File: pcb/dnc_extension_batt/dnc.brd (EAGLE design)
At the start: 97.2 x 88 mm, 132 parts, among them IC1 LM2596S, IC2 74S244DW, Q1 IRF9321PBF, Q10 BSS316, Q11 BSS316, Q12 BSS138, Q13 BSS138, Q2 BSS670, Q3 BSS138, Q4 BSS670, Q5 BSS138, Q6 BSS670, Q7 BSS138, Q8 BSS138, Q9 BSS670, U1 MAX202CDWR, U2 74HCT595D, U3 TC7SU04F, U4 AL8807, U5 AL8807, U6 TC7SU04F

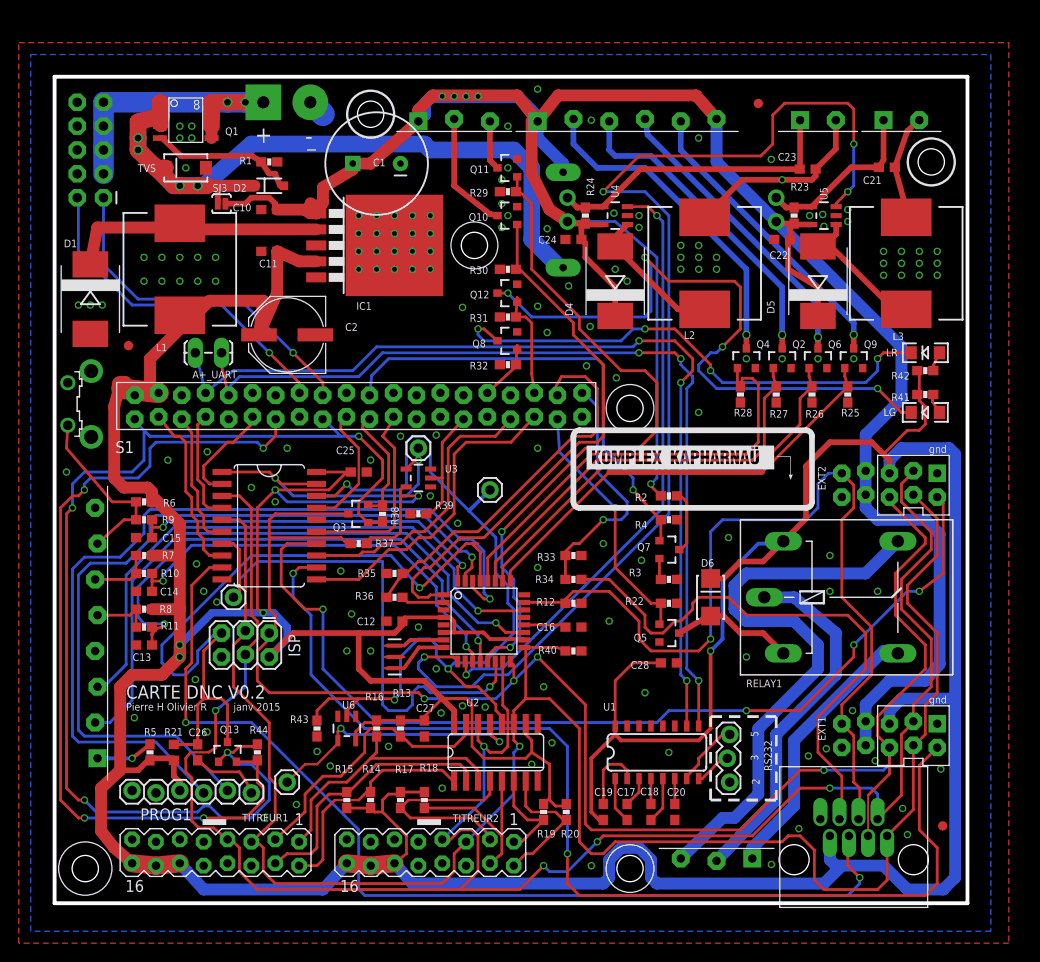
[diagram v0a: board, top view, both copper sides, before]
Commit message: carte extension chargeur LIPO
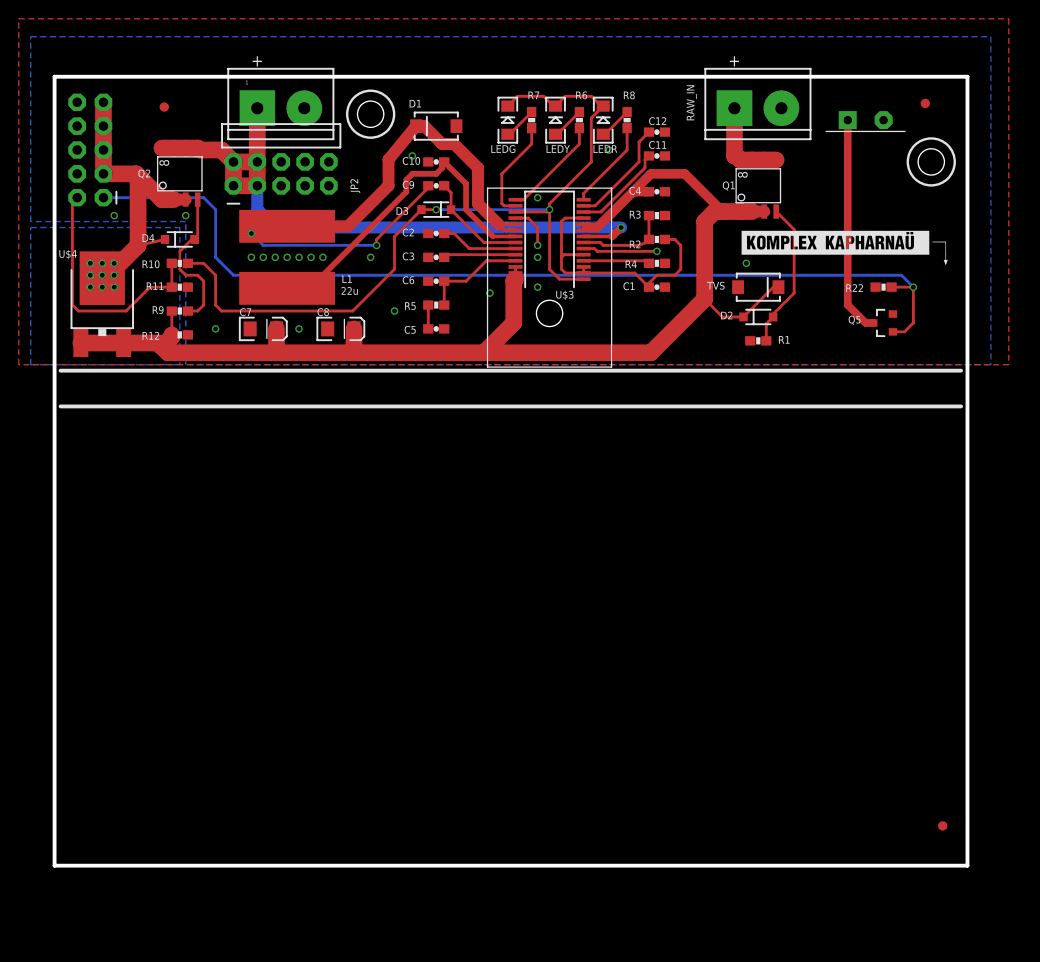
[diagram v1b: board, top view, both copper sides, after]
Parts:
- removed 16MHZ: 16MHZ, SparkFun-FreqCtrl:RESONATOR-SMD
- removed A+_UART: (no value), SparkFun:1X02_LOCK_LONGPADS
- removed AT328: ATMEGA328, SparkFun:TQFP32-08
- removed C13, C14, C15, C21, C23: 1uF, rcl:C0603
- removed C16, C17, C18, C19, C20, C22, C24, C25, C26, C27, C28: 0.1uF, rcl:C0603
- removed D5: 40v5A, diode:SMC
- removed D6: (no value), SparkFun-DiscreteSemi:SMA-DIODE_ALT
- removed EXT1: EXT1, pierre_vv:EXTPINDNC
- removed EXT2: EXT2, pierre_vv:EXTPINDNC
- removed F1: 8A, SparkFun:PTC
- removed IC1: LM2596S, national-semiconductor:TO263-5
- removed IC2: 74S244DW, 74xx-us:SO20W
- removed ISP: AVR_SPI_PRG_62X3_LOCK, SparkFun:2X3_LOCK
- removed JP3: atmega cs, SparkFun-Connectors:1X01
- removed JP4: allcs, SparkFun-Connectors:1X01
- removed JP5: OE 595, SparkFun-Connectors:1X01
- removed L2, L3: 100nH, SparkFun:CDRH125
- removed LG, LR: (no value), SparkFun-LED:LED-1206
- removed PLUG_3.81_1: FLEX, pierre_vv:PLUG_03
- removed PLUG_3.81_2: RELAY, pierre_vv:PLUG_03
- removed PLUG_3.81_2_2: LED10W1, pierre_vv:PLUG_02
- removed PLUG_3.81_6_1: GYRO LED, pierre_vv:PLUG_06
- removed PROG1: (no value), SparkFun:1X06_LOCK
- removed Q10, Q11: BSS316, SparkFun-DiscreteSemi:SOT23-3
- removed Q12, Q13, Q3, Q7, Q8: BSS138, SparkFun-DiscreteSemi:SOT23-3
- removed Q4, Q6, Q9: BSS670, SparkFun-DiscreteSemi:SOT23-3
- removed R13, R14, R15, R16, R17, R18, R19, R20, R25, R26, R27, R28, R29, R30, R31, R32: 100K, SparkFun-Passives:0603-RES
- removed R21: 10K, rcl:R0603
- removed R23, R24: 0.110, SparkFun-Passives:0603-RES
- removed R33, R35: 20K, SparkFun-Passives:0603-RES
- removed R34, R36, R37, R38, R39, R40, R43, R44: 10K, SparkFun-Passives:0603-RES
- removed R41, R42: 220, SparkFun-Passives:0603-RES
- removed RELAY1: G5L, relay:G5LE
- removed RS232: (no value), SparkFun-Connectors:1X03_LOCK
- removed S1: (no value), switch-omron:B3F-31XX
- removed SJ1, SJ2: JUMPER-PTH-2-NO, SparkFun-Passives:PTH-JUMPER-2-NO_NO_SILK
- removed SJ3: JUMPER-PAD-2-NC_BY_PASTE, SparkFun-Passives:PAD-JUMPER-2-NC_BY_PASTE_YES_SILK
- removed TITREUR1, TITREUR2: DNC_TITREUR, pierre_vv:DNC_TITREUR
- removed U$6: M08, pierre_vv:PLUG_08
- removed U$8: RJ45-EXTDNC, con-amphenol-rj45-ld:RJ45-TRAFO
- removed U1: MAX202CDWR, SparkFun-DigitalIC:SO016
- removed U2: 74HCT595D, IC:SO16
- removed U3, U6: TC7SU04F, SparkFun-DigitalIC:SOT23-5
- removed U4, U5: AL8807, SparkFun-PowerIC:SOT23-5
- added 1: BATT, pierre_vv:DNC_IN2_PWR
- added C3, C4, C5, C9: 0.1u, SparkFun-Passives:0603-CAP
- added C6: 1n, SparkFun-Passives:0603-CAP
- added C7, C8: 22u, SparkFun-Passives:EIA3216
- added D3: 1N4148W, SparkFun-DiscreteSemi:SOD-123
- added LEDG, LEDR, LEDY: (no value), SparkFun-LED:LED-1206
- added U$3: MAX1758, pierre_vv:SSOP28
- C1: value 680uF30mm -> 1u; device SparkFun:CPOL-RADIAL-1000UF-25V -> SparkFun-Passives:0603-CAP
- C10: value 0.1uF -> 0.1u; device rcl:C0603 -> SparkFun-Passives:0603-CAP
- C11: value 0.1uF -> 2.2n; device rcl:C0603 -> SparkFun-Passives:0603-CAP
- C12: value 0.1uF -> 4.7n; device rcl:C0603 -> SparkFun-Passives:0603-CAP
- C2: value 220u -> 0.1u; device rcl:PANASONIC_E -> SparkFun-Passives:0603-CAP
- D1: value 40v5A -> B330; device diode:SMC -> SparkFun-DiscreteSemi:SMA-DIODE
- D2: value 10V -> 10v
- D4: value 40v5A -> 10v; device diode:SMC -> SparkFun-DiscreteSemi:SOD-123
- JP2: value regrck -> BATT; device SparkFun-Connectors:1X01 -> SparkFun-Connectors:2X5-RA
- L1: value 68nH3A -> 22u; device SparkFun:CDRH125 -> pierre_vv:SRN1060
- PLUG_3.81_2_1: value LED10W2 -> RELAY-SINK
- Q2: value BSS670 -> IRF9321PBF; device SparkFun-DiscreteSemi:SOT23-3 -> pierre_vv:SO-8
- R10, R11: value 33K -> 10K
- R12: value (none) -> 10K
- R2: value 100k1% -> 100K1%
- R3: value 10k1% -> 100K1%
- R4: value 100K -> 10K
- R5: value 1K -> 10K
- R6, R7, R8: value 56K -> 1K
- R9: value 33K -> 100K
- RAW_IN: value DNC_IN2PWR -> SUPPLY
- U$4: value RASPIA+ -> 45V10A; device pierre_vv:RASPIA+ -> pierre_vv:DPAK
- moved U$4 88.1 mm to (5.08, 61.0), turned to 0 degrees
- moved R8 73.2 mm to (61.0, 79.4), turned to 90 degrees
- moved Q2 67.1 mm to (13.3, 73.7), turned to 90 degrees
- moved TVS 62.3 mm to (74.9, 61.6), turned to 0 degrees
- moved R7 62.1 mm to (50.8, 79.4), turned to 90 degrees
- moved R6 61.6 mm to (55.9, 79.4), turned to 90 degrees
- moved Q1 61.4 mm to (74.9, 72.4), turned to 90 degrees
- moved C12 59.1 mm to (64.1, 78.1), turned to 0 degrees
- moved R5 56.5 mm to (40.6, 59.7), turned to 0 degrees
- moved R1 55.4 mm to (74.9, 55.9), turned to 180 degrees
- moved D2 53.9 mm to (74.9, 58.4)
- moved R12 50.7 mm to (13.3, 56.5)
- moved RAW_IN 50.2 mm to (72.4, 80.6), flipped to the top, turned to 0 degrees
- moved D4 46.6 mm to (13.3, 66.7), turned to 0 degrees
- moved C11 42.5 mm to (64.1, 75.6), turned to 0 degrees
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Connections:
- removed net +3V3: Q13.1, Q3.1, R38.2, R44.2, U$4.1, U$4.17
- removed net +5V: AT328.18, AT328.4, AT328.6, C11.1, C12.1, C19.1, C2.+, C25.1, C27.1, C28.1, D6.C, EXT1.5V, EXT2.5V, IC1.4, IC2.20, ISP.2, L1.2, PROG1.4, R13.2, R14.2, R15.2, R16.2, R17.2, R18.2, R19.2, R20.2, R21.2, R37.2, R41.2, R42.2, R5.2, R6.2, R7.2, R8.2, RELAY1.2, TITREUR1.12, TITREUR1.14, TITREUR1.16, TITREUR2.12, TITREUR2.14, TITREUR2.16, U$4.2, U$4.4, U$8.1, U1.16, U2.10, U2.16, U3.5, U6.5
- removed net /REG_RCK_5V=ACTIVE_CS: JP5.1, U2.13, U6.4
- removed net ALL_CS_ENABLE_ACTIVE_LOW_5V: IC2.1, IC2.19, JP4.1, U3.4
- removed net ANALOG_BAT: AT328.24
- removed net ANALOG_RAW: Q7.2, R3.2
- removed net AREF: AT328.20, C16.1
- removed net ATMEGA_CS: IC2.13, U$4.33
- removed net ATMEGA_CS_5V: AT328.14, IC2.7, JP3.1
- removed net CODE: AT328.23, EXT1.RETOURANALOG, EXT2.RETOURANALOG, R12.1, U$8.6
- removed net CS_TRIGGER_ACTIVE_HIGH: R39.2, U$4.29, U3.2
- removed net DTR: C26.1, PROG1.1
- removed net EXT1_CS: IC2.8, U$4.3
- removed net EXT1_CS_5V: EXT1./CS, IC2.12
- removed net EXT2_CS: IC2.6, U$4.5
- removed net EXT2_CS_5V: EXT2./CS, IC2.14
- removed net EXT3_CS: IC2.4, U$4.7
- removed net EXT3_CS_5V: IC2.16
- removed net FLOAT1: AT328.19, U$6.2
- removed net FLOAT2: AT328.22, U$6.3
- removed net GYRO_1: AT328.28, Q4.1, R28.2
- removed net GYRO_2: AT328.27, Q2.1, R27.2
- removed net GYRO_3: AT328.26, Q6.1, R26.2
- removed net GYRO_4: AT328.25, Q9.1, R25.2
- removed net INT_ATMEGA: R35.2, R36.1, U$4.38
- removed net INT_ATMEGA_5V: AT328.2, R36.2
- removed net INT_TELECO: R33.2, R34.1, U$4.40
- removed net INT_TELECO_5V: R34.2, U$8.4
- removed net LED+1: C23.1, PLUG_3.81_2_1.1, R24.1, SJ1.2, U4.4
- removed net LED+2: C21.1, PLUG_3.81_2_2.1, R23.1, SJ2.2, U5.4
- removed net LED-1: C23.2, L2.2, PLUG_3.81_2_1.2
- removed net LED-2: C21.2, L3.2, PLUG_3.81_2_2.2
- removed net LEDR: LR.C, Q8.3
- removed net LED_G: Q12.1, R31.2, U$4.36
- removed net LED_R: Q8.1, R32.2, U$4.32
- removed net LG: LG.C, Q12.3
- removed net MISO: Q3.2, R38.1, U$4.21
- removed net MISO_5V: AT328.16, EXT1.MISO, EXT2.MISO, ISP.1, Q3.3, R37.1, U$8.5
- removed net MOSI: IC2.17, U$4.19
- removed net MOSI_5V: AT328.15, EXT1.MOSI, EXT2.MOSI, IC2.3, ISP.4, TITREUR1.7, TITREUR2.7, U$8.8, U2.14
- removed net N$22: R6.1, R9.1, S1.2, U$6.7
- removed net N$23: R11.1, R8.1, U$6.5
- removed net N$24: C19.2, U1.2
- removed net N$25: R5.1, U$6.1
- removed net N$35: C20.1, U1.6
- removed net N$43: 16MHZ.1, AT328.7
- removed net N$44: 16MHZ.3, AT328.8
- removed net N$50: C18.2, U1.5
- removed net N$51: C18.1, U1.4
- removed net N$52: C17.2, U1.3
- removed net N$53: C17.1, U1.1
- removed net PRXD_PIN2_RS232: RS232.1, U1.7
- removed net PTXD_PIN3_RS232: RS232.2, U1.8
- removed net PUSH1: AT328.32, C15.1, R9.2
- removed net PUSH2: AT328.11, C14.1, R10.2
- removed net PUSH3: AT328.12, C13.1, R11.2
- removed net PWM_FLEX_1: AT328.1, Q10.1, R30.2
- removed net PWM_FLEX_2: AT328.13, Q11.1, R29.2
- removed net PWM_LED_1: AT328.9, U5.3
- removed net PWM_LED_2: AT328.10, U4.3
- removed net RAW_FUSED: C1.1, C10.1, C22.1, C24.1, D4.C, D5.C, EXT1.RAW, EXT1.RAW2, EXT2.RAW, EXT2.RAW2, F1.P$2, IC1.1, PLUG_3.81_1.1, PLUG_3.81_6_1.1, PLUG_3.81_6_1.6, R2.2, R23.2, R24.2, SJ1.1, SJ2.1, SJ3.2, U4.5, U5.5
- removed net RAW_UNPROTECTED: JP1.3, JP1.5, JP1.7, JP1.9, Q1.5, Q1.6, Q1.7, Q1.8, RAW_IN.1
- removed net READ_BATTERY: Q7.1, R4.2, U$4.22
- removed net REG_RCK: IC2.2, U$4.11
- removed net REG_RCK_5V: IC2.18, JP2.1, R43.2, U2.12, U6.2
- removed net RELAY1: Q5.1, R22.2, U$4.37
- removed net RESET: Q13.2, R44.1, U$4.13
- removed net RESET_5V: AT328.29, C26.2, ISP.5, Q13.3, R21.1
- removed net RST1: R16.1, TITREUR1.1, U2.3
- removed net RST2: R14.1, TITREUR1.2, U2.1
- removed net RST3: R13.1, TITREUR1.3, U2.15
- removed net RST4: R15.1, TITREUR1.4, U2.2
- removed net RST5: R19.1, TITREUR2.1, U2.6
- removed net RST6: R20.1, TITREUR2.2, U2.7
- removed net RST7: R17.1, TITREUR2.3, U2.4
- removed net RST8: R18.1, TITREUR2.4, U2.5
- removed net RX-I: AT328.30, PROG1.3
- removed net RXA+: A+_UART.2, U$4.10, U1.9
- removed net SCK: IC2.15, U$4.23
- removed net SCK_5V: AT328.17, EXT1.SCK, EXT2.SCK, IC2.5, ISP.3, R40.2, TITREUR1.5, TITREUR2.5, U$8.7, U2.11
- removed net TELECO_CS: IC2.11, U$4.35
- removed net TELECO_CS_5V: IC2.9, U$8.3
- removed net TX-O: AT328.31, PROG1.2
- removed net TXA+: A+_UART.1, U$4.8, U1.10
- new net N$17: C9.1, D3.C, U$3.22
- new net N$19: PLUG_3.81_2_1.1, Q5.3
- new net N$5: R4.1, U$3.4
- new net RAW_UNPROTECTED1: Q1.5, Q1.6, Q1.7, Q1.8, RAW_IN.1
- new net SYSTEM_LOAD: D4.C, JP1.3, JP1.5, JP1.7, JP1.9, Q2.1, Q2.2, Q2.3, U$4.4
- new net V+BATT: 1.1, JP2.1, JP2.2, JP2.3, JP2.4, Q2.5, Q2.6, Q2.7, Q2.8, U$3.8
- new net VL: D3.A, LEDG.C, LEDR.C, LEDY.C, R10.2, U$3.1, U$3.17
- net CHARGING: now also R10.1, R11.2; no longer U$4.16
- net GND: now also 1.2, C1.1, C2.2, C3.2, C4.1, C5.2, C6.2, C7.C, C8.C, JP2.10, JP2.7, JP2.8, JP2.9, PLUG_3.81_2_1.2, R11.1, R4.2, U$3.18, U$3.6; no longer 16MHZ.2, AT328.21, AT328.3, AT328.5, C1.2, C13.2, C14.2, C15.2, C16.2, C2.-, C20.2, C22.2, C24.2, C25.2, C27.2, C28.2, EXT1.1_GND, EXT1.GND2, EXT2.1_GND, EXT2.GND2, IC1.3, IC1.5, IC1.THERMAL, IC2.10, ISP.6, PROG1.5, PROG1.6, Q10.2, Q11.2, Q12.2, Q2.2, Q4.2, Q6.2, Q8.2, Q9.2, R25.1, R26.1, R27.1, R28.1, R29.1, R30.1, R31.1, R32.1, R33.1, R35.1, R39.1, R4.1, R40.1, R43.1, RS232.3, S1.1, TITREUR1.11, TITREUR1.13, TITREUR1.15, TITREUR1.8, TITREUR2.11, TITREUR2.13, TITREUR2.15, TITREUR2.8, U$4.14, U$4.20, U$4.25, U$4.30, U$4.34, U$4.39, U$4.6, U$4.9, U$6.4, U$6.8, U$8.2, U1.15, U2.8, U3.3, U4.2, U5.2, U6.3
- net N$1: now also C1.2, R2.1, U$3.11, U$3.2, U$3.3, U$3.5; no longer D1.C, IC1.2, L1.1
- net N$10: now also R6.1, U$3.15; no longer PLUG_3.81_6_1.2, Q4.3
- net N$11: now also R7.1, U$3.16; no longer PLUG_3.81_6_1.3, Q2.3
- net N$12: now also R8.1, U$3.14; no longer PLUG_3.81_6_1.4, Q6.3
- net N$13: now also LEDY.A, R6.2; no longer PLUG_3.81_6_1.5, Q9.3
- net N$14: now also LEDG.A, R7.2; no longer PLUG_3.81_1.2, Q10.3
- net N$15: now also LEDR.A, R8.2; no longer PLUG_3.81_2.3, RELAY1.O
- net N$16: now also C11.1, U$3.12; no longer D6.A, Q5.3, RELAY1.1
- net N$18: now also C10.1, L1.P$2, U$3.21; no longer LG.A, R41.1
- net N$20: now also D4.A, Q2.4, R9.1; no longer R10.1, R7.1, U$6.6
- net N$21: now also C12.1, U$3.13; no longer LR.A, R42.1
- net N$3: now also C9.2, D1.C, L1.P$1, U$3.19, U$3.20; no longer Q7.3, R2.1
- net N$4: now also R2.2, R3.2, U$3.7; no longer PLUG_3.81_2.1, RELAY1.S
- net N$6: now also C5.1, R5.1; no longer D4.A, L2.1, U4.1
- net N$7: now also C2.1, U$3.23; no longer D5.A, L3.1, U5.1
- net N$8: now also C3.1, U$3.24; no longer PLUG_3.81_2.2, RELAY1.P
- net N$9: now also C6.1, R5.2, U$3.25; no longer PLUG_3.81_1.3, Q11.3
- net RAW_POL_PROTECTED: now also C4.2, C7.A, C8.A, R12.1, R9.2, U$3.10, U$3.26, U$3.27, U$3.28, U$3.9, U$4.1, U$4.3; no longer F1.P$1MOV, SJ3.1
- net RELAY_CHARGE_BOARD: now also Q5.1, R22.2; no longer U$4.18
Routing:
- net +5V: track 568.4 -> 0.00 mm, vias 6 -> 0
- net RAW_FUSED: track 262.9 -> 0.00 mm, vias 5 -> 0
- net MOSI_5V: track 209.3 -> 0.00 mm, vias 5 -> 0
- net SCK_5V: track 202.2 -> 0.00 mm, vias 1 -> 0
- net MISO_5V: track 171.6 -> 0.00 mm, vias 4 -> 0
- net PWM_LED_1: track 124.0 -> 0.00 mm, vias 4 -> 0
- net +3V3: track 123.9 -> 0.00 mm, vias 4 -> 0
- net EXT1_CS_5V: track 115.9 -> 0.00 mm, vias 2 -> 0
- net TELECO_CS_5V: track 108.2 -> 0.00 mm, vias 2 -> 0
- net EXT2_CS_5V: track 103.6 -> 0.00 mm, vias 4 -> 0
- net TXA+: track 99.1 -> 0.00 mm, vias 3 -> 0
- net RXA+: track 96.1 -> 0.00 mm, vias 3 -> 0
- net CODE: track 95.7 -> 0.00 mm, vias 1 -> 0
- net RX-I: track 92.2 -> 0.00 mm, vias 1 -> 0
- net RESET: track 90.9 -> 0.00 mm, vias 4 -> 0
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- added copper zone on layer 16, net SYSTEM_LOAD
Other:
- board size 97.2 x 88 mm -> 97.2 x 84 mm
- board text added: "BATT+"
- board text added: "DNC carte batterie V0"
- board text added: "GND"
- board text added: "Pierre H Olivier R Jan 2015"
- board text added: "Relay -"
- board text added: "SUPPLY"
- board text removed: "2"
- board text removed: "3"
- board text removed: "5"
- board text removed: "CARTE DNC V0.2"
- board text removed: "Pierre H Olivier R"
- board text removed: "janv 2015"

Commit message: add remote + enclosure
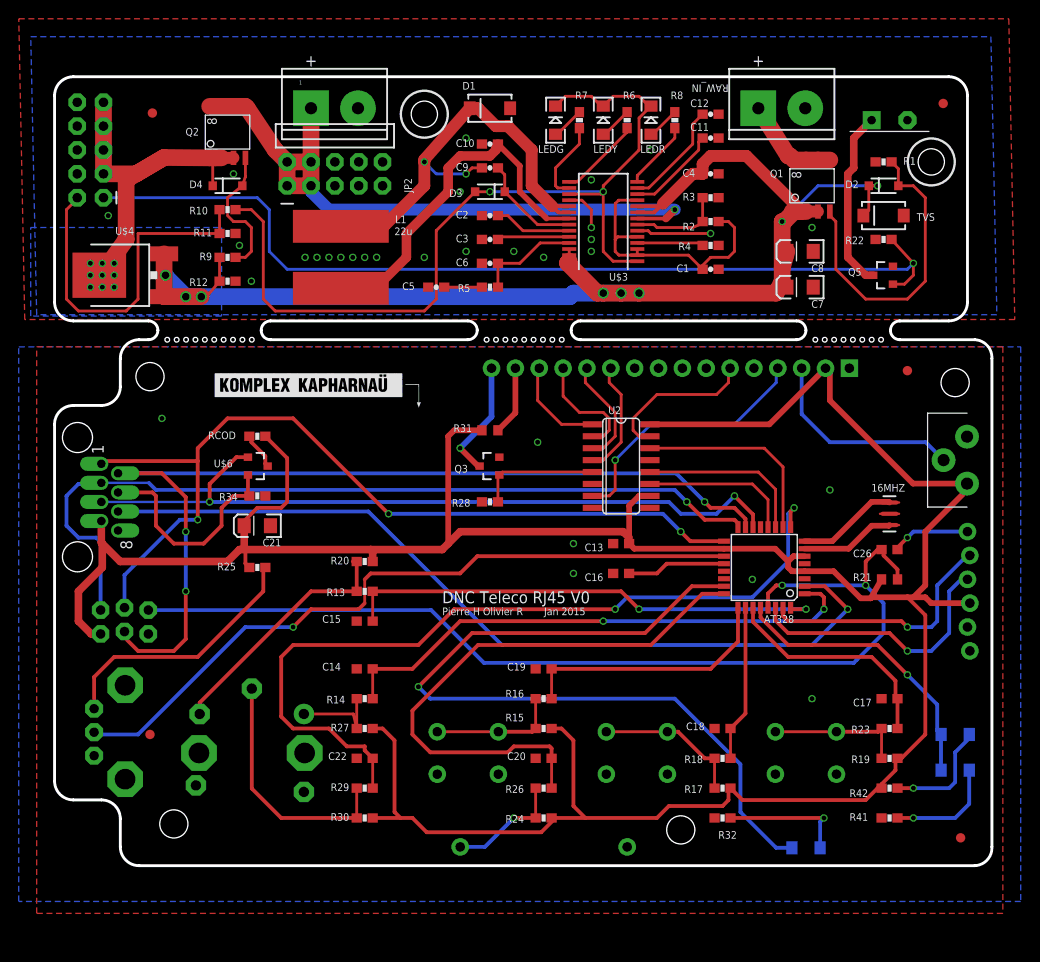
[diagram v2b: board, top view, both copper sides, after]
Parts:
- added 16MHZ: 16MHZ, SparkFun-FreqCtrl:RESONATOR-SMD
- added AT328: ATMEGA328, SparkFun:TQFP32-08
- added C13, C16, C26: 0.1uF, rcl:C0603
- added C14, C15: 10n, rcl:C0603
- added C17, C18, C19, C20, C22: 1uF, rcl:C0603
- added C21: 22u, SparkFun-Passives:EIA3216
- added ISP: AVR_SPI_PRG_62X3_LOCK, SparkFun:2X3_LOCK
- added JP3, JP4: FIDUCIAL1X2.5, SparkFun:FIDUCIAL-1X2.5
- added LG, LG1, LR-HIGH: (no value), SparkFun-LED:LED-1206
- added PROG1: (no value), SparkFun:1X06_LOCK
- added Q3: BSS138, SparkFun-DiscreteSemi:SOT23-3
- added R13, R14, R20, R27: 10K, SparkFun-Passives:0603-RES
- added R15, R17, R19, R24, R30: 56K, SparkFun-Passives:0603-RES
- added R16, R18, R23, R26, R29: 33K, SparkFun-Passives:0603-RES
- added R21: 10K, rcl:R0603
- added R25, R32, R41: 1K, SparkFun-Passives:0603-RES
- added R28: 100K, SparkFun-Passives:0603-RES
- added R31: 5, rcl:R0603
- added R34: 5.1K, SparkFun-Passives:0603-RES
- added R42: 100, SparkFun-Passives:0603-RES
- added RCOD: 270, SparkFun-Passives:0603-RES
- added REED: SWITCH-MOMENTARY-2PTH_REED, SparkFun-Electromechanical:REED_SWITCH_PTH
- added S1, S2, S3: (no value), SparkFun:TACTILE-PTH
- added U$5: BOITIERBOITIER_FARNELLE_479-0020-0, pierre_vv:BOX_SIZE
- added U$6: MOSFET-PCHANNEL, SparkFun-DiscreteSemi:SOT23-3
- added U$6MOV: LOGO, pierre_vv:KXKMLOGO
- added U$7: ROTARYEC12D1564404, pierre_vv:ROTARY_ALPS_EC12
- added U$8: RJ45-EXTDNC, con-amphenol-rj45-ld:RJ45-TRAFO
- added U$9: POT, pierre_vv:POT_ALPS
- added U1: LCD-16X2NOHOLES, SparkFun-Displays:LCD-16X2_NOHOLES
- added U2: 74HCT595D, IC:SO16
- U$1: value RADIATEUR -> POTTRIMER-TE-CB10H; device pierre_vv:RADIATEUR_577102B00000G -> pierre_vv:TRIMER-TE
- moved C7 57.3 mm to (79.4, 61.6), turned to 180 degrees
- moved C8 49.6 mm to (79.4, 65.4), turned to 180 degrees
- moved U$1 47.1 mm to (97.2, 43.2), turned to 90 degrees
- moved R1 23.3 mm to (88.3, 74.9)
- moved U$2 22.6 mm to (63.5, 80.0), flipped to the bottom
- moved D2 19.3 mm to (88.3, 72.4)
- moved TVS 15.4 mm to (88.3, 69.2), turned to 180 degrees
- moved D4 7.65 mm to (18.4, 72.4)
- moved R11 7.65 mm to (18.4, 67.3)
- moved R12 7.65 mm to (18.4, 62.2)
- moved R9 7.65 mm to (18.4, 64.8)
- moved R10 7.65 mm to (18.4, 69.8)
- moved Q2 6.75 mm to (18.4, 78.1)
- moved U$3 6.02 mm to (58.4, 68.6)
- moved C6 6.02 mm to (46.4, 64.1)
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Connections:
- new net +5V: AT328.18, AT328.4, AT328.6, C13.1, C21.A, ISP.2, PROG1.4, R15.2, R17.2, R19.2, R20.1, R21.2, R24.2, R25.2, R27.1, R30.1, R31.2, R42.2, RCOD.1, U$1.1, U$8.1, U1.2, U2.10, U2.16
- new net ANALOG1: AT328.19, U$9.2
- new net AREF: AT328.20, C16.1
- new net CODE: R34.1, U$6.2, U$8.6
- new net DTR: C26.1, PROG1.1
- new net INT_TELECO_5V: AT328.2, U$8.4
- new net LCD-D4: U1.11, U2.4
- new net LCD-D5: U1.12, U2.3
- new net LCD-D6: U1.13, U2.2
- new net LCD-D7: U1.14, U2.1
- new net LCD-E: U1.6, U2.15
- new net LCD-LED-CONTROL: Q3.1, R28.2, U2.5
- new net LCD-RCK: AT328.11, U2.12
- new net LCD-RS: U1.4, U2.7
- new net LCD-SCK: AT328.12, U2.11
- new net LCD-SER: AT328.10, U2.14
- new net LED-PUSH3: AT328.23, LG1.C
- new net MISO_5V: AT328.16, ISP.1, U$8.5
- new net MOSI_5V: AT328.15, ISP.4, U$8.8
- new net N$22: R15.1, R16.1, S1.1, S1.2
- new net N$23: R14.1, R27.2, U$7.A
- new net N$24: R17.1, R18.1, S2.1, S2.2
- new net N$25: R13.1, R20.2, U$7.B
- new net N$26: R19.1, R23.1, S3.1, S3.2
- new net N$27: R25.1, U$9.3
- new net N$28: R24.1, R26.1, REED.P$1
- new net N$29: LR-HIGH.A, R42.1
- new net N$30: LG.A, R41.1
- new net N$31: R29.2, R30.2, U$7.E
- new net N$32: R31.1, U1.15
- new net N$33: U$1.2, U1.3
- new net N$34: Q3.3, U1.16
- new net N$35: LG1.A, R32.1
- new net N$36: RCOD.2, U$6.3
- new net N$38: AT328.13
- new net N$43: 16MHZ.1, AT328.7
- new net N$44: 16MHZ.3, AT328.8
- new net PUSH1: AT328.25, C19.1, R16.2
- new net PUSH2: AT328.26, C18.1, R18.2
- new net PUSH3: AT328.27, C17.1, R23.2
- new net REED: AT328.24, C20.1, R26.2
- new net RESET_5V: AT328.29, C26.2, ISP.5, R21.1
- new net ROTARY-A: AT328.32, C15.1, R13.2
- new net ROTARY-B: AT328.1, C14.1, R14.2
- new net ROTARY-SW: AT328.9, C22.1, R29.1
- new net RX-I: AT328.30, PROG1.3
- new net SCK_5V: AT328.17, ISP.3, U$8.7
- new net TELECO_CS_5V: AT328.14, U$6.1, U$8.3
- new net TX-O: AT328.31, PROG1.2
- new net WARNING: AT328.28, LG.C, LR-HIGH.C
- net GND: now also 16MHZ.2, AT328.21, AT328.3, AT328.5, C13.2, C14.2, C15.2, C16.2, C17.2, C18.2, C19.2, C20.2, C21.C, C22.2, ISP.6, PROG1.5, PROG1.6, Q3.2, R28.1, R32.2, R34.2, R41.2, REED.P$2, S1.3, S1.4, S2.3, S2.4, S3.3, S3.4, U$1.3, U$7.C, U$7.D, U$8.2, U$9.1, U1.1, U1.5, U2.13, U2.8
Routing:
- net +5V: track 0.00 -> 321.8 mm
- net RESET_5V: track 0.00 -> 108.7 mm, vias 0 -> 2
- net MOSI_5V: track 0.00 -> 101.3 mm, vias 0 -> 3
- net SCK_5V: track 0.00 -> 94.6 mm, vias 0 -> 3
- net INT_TELECO_5V: track 0.00 -> 90.8 mm, vias 0 -> 1
- net MISO_5V: track 0.00 -> 89.0 mm, vias 0 -> 1
- net ROTARY-SW: track 0.00 -> 87.7 mm, vias 0 -> 2
- net LED-PUSH3: track 0.00 -> 86.8 mm, vias 0 -> 1
- net TELECO_CS_5V: track 0.00 -> 80.1 mm, vias 0 -> 2
- net ANALOG1: track 0.00 -> 77.2 mm, vias 0 -> 1
- net REED: track 0.00 -> 61.1 mm
- net ROTARY-B: track 0.00 -> 57.3 mm, vias 0 -> 2
- net ROTARY-A: track 0.00 -> 51.8 mm, vias 0 -> 2
- net WARNING: track 0.00 -> 30.8 mm, vias 0 -> 1
- net RX-I: track 0.00 -> 28.9 mm, vias 0 -> 1
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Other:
- board size 97.2 x 84 mm -> 99.8 x 56 mm
- board text added: "A"
- board text added: "B"
- board text added: "DNC Teleco RJ45 V0"
- board text added: "OK"
- board text added: "RPI + 8mm"
- board text added: "RPI+ 10mm"
- board text added: "SELECT"
- board text added: "contrast"
- board text added: "gnd"

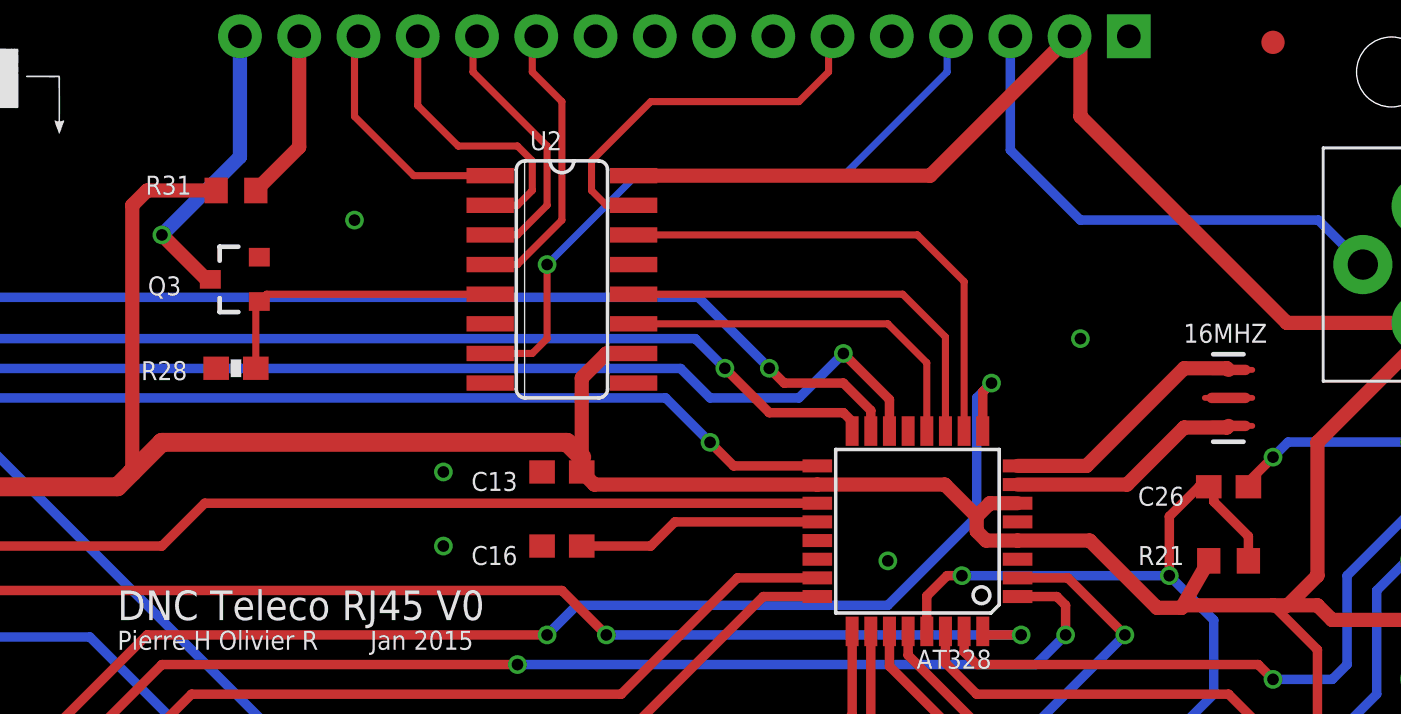
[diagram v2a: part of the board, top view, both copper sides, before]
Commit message: BOM ext teleco et chargeur
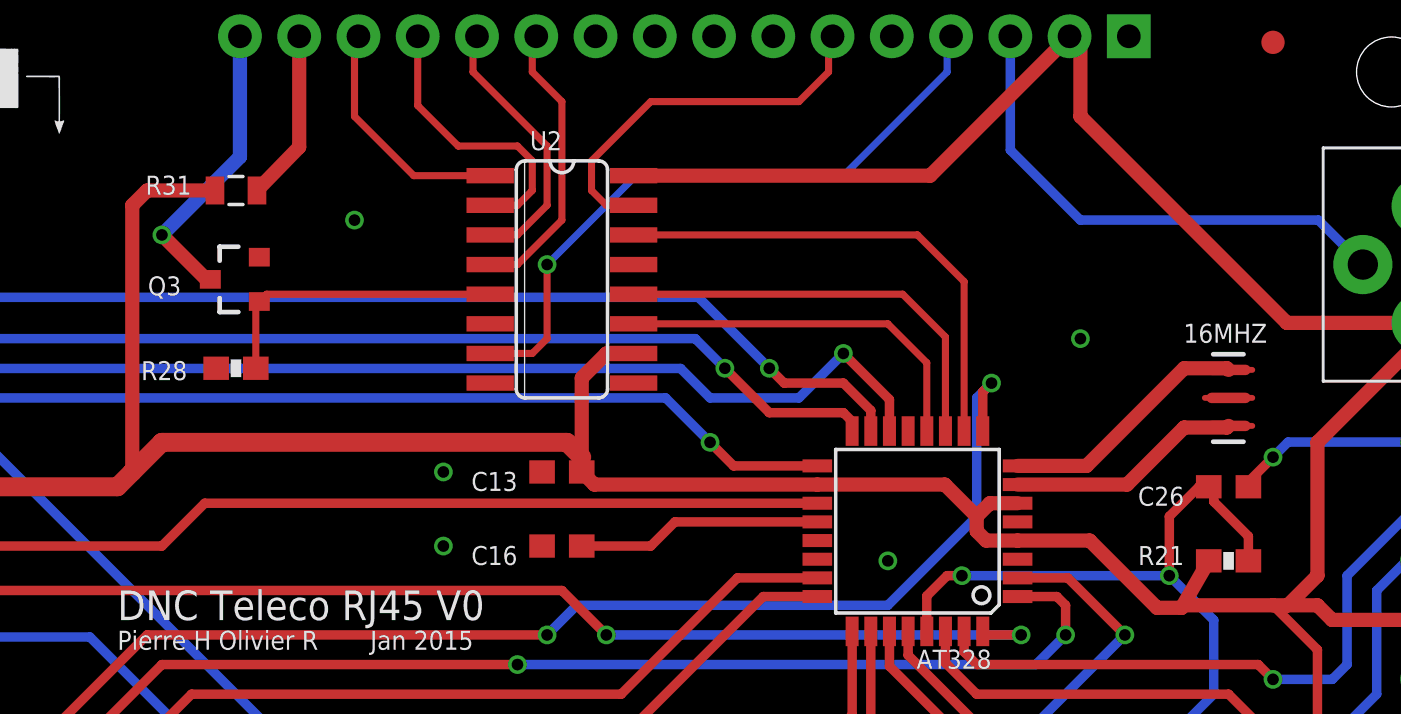
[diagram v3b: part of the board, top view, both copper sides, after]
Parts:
- L4: value (none) -> LR-HIGH
- L5, L6: value (none) -> LG
- R21: device rcl:R0603 -> SparkFun-Passives:0603-RES
- R31: device rcl:R0603 -> SparkFun-Passives:0805
- renumbered LG to L5, LG1 to L6, LR-HIGH to L4
